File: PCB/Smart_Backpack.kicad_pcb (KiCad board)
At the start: 2 copper layers, 65.8 x 74.4 mm, 58 parts, among them J1 Conn_01x03_Pin, J2 Conn_01x02_Pin, J3 Conn_01x02_Pin, J4 Conn_01x03_Pin, J5 Conn_01x03_Pin, J6 Conn_01x03_Pin, J7 Conn_01x07_Pin, J8 Conn_01x08_Socket, J9 USB_C_Receptacle_USB2.0_16P, SW1 SW_Push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

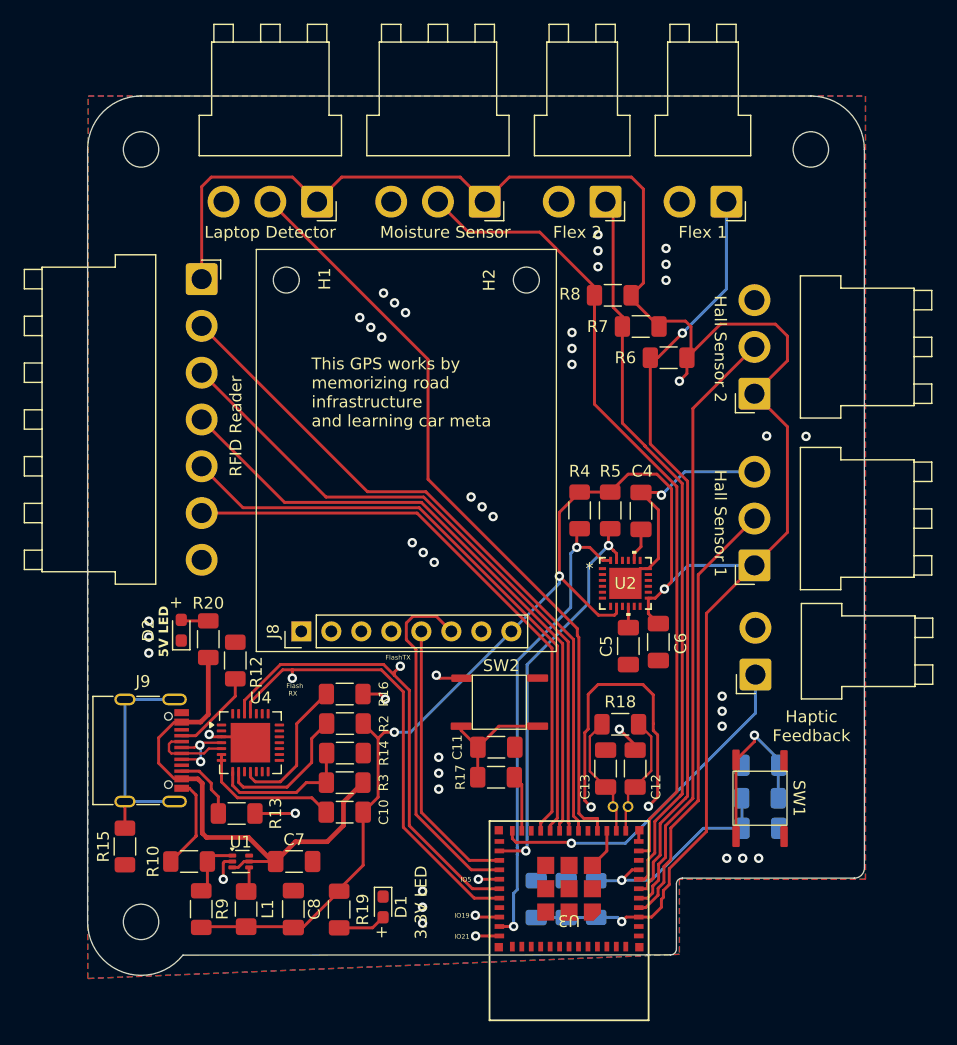
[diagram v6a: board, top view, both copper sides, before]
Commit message: fix silkscreen for motor connector
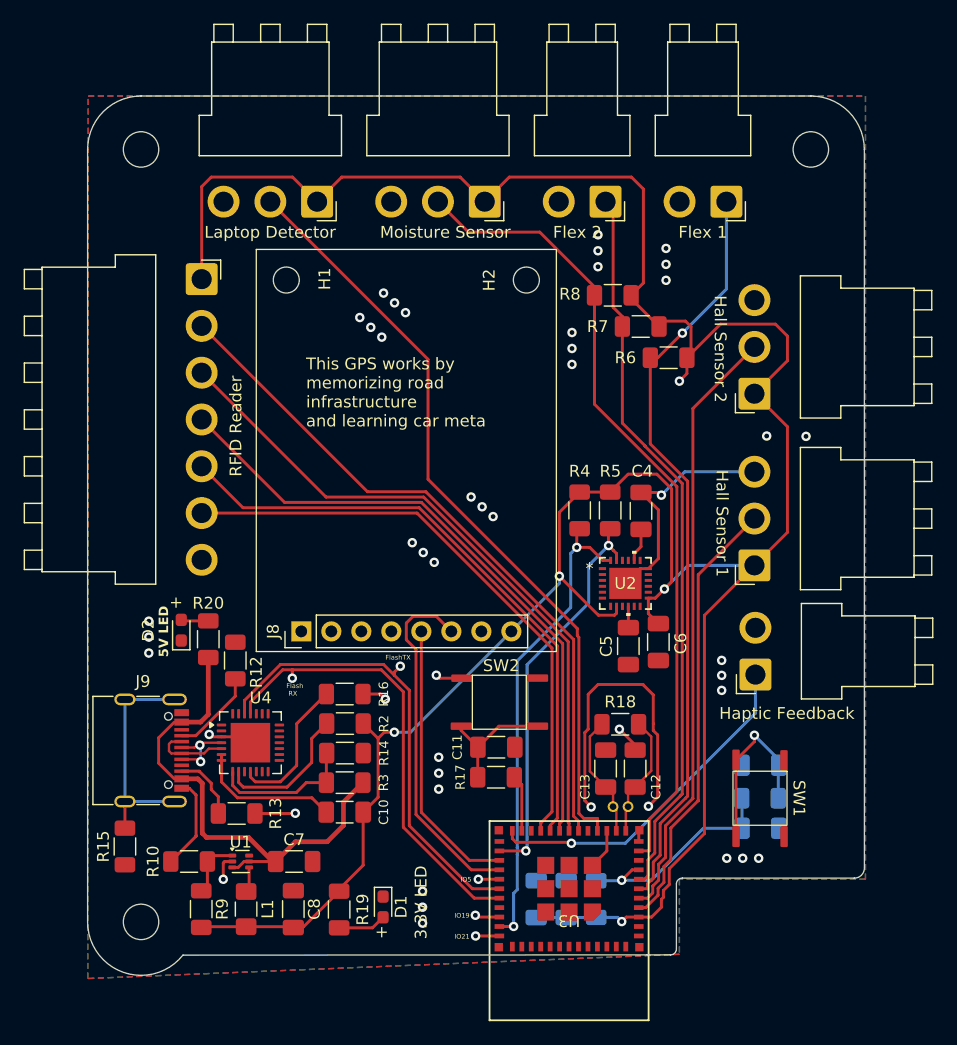
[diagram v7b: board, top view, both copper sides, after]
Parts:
- J10: renamed from Haptic Feedback
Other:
- board text removed: "Haptic Feedback"
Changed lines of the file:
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@@
 		)
 		(property "Label" "Hall Sensor 1"
-			(at 3.5536 -2.8956 270)
+			(at 3.5536 -2.742 270)
 			(unlocked yes)
 			(layer "F.SilkS")
@@
 		(descr "JST VH series connector, B2PS-VH (http://www.jst-mfg.com/product/pdf/eng/eVH.pdf), generated with kicad-footprint-generator")
 		(tags "connector JST VH horizontal")
-		(property "Reference" "Haptic Feedback"
+		(property "Reference" "J10"
 			(at -3.862 3.473 0)
 			(layer "F.SilkS")
@@
 			(at 1.98 16.1 90)
 			(layer "F.Fab")
+			(hide yes)
 			(effects
 				(font
@@
 			)
 		)
+		(property "Label" "Haptic Feedback"
+			(at -3.286 2.665 0)
+			(unlocked yes)
+			(layer "F.SilkS")
+			(effects
+				(font
+					(size 1 1)
+					(thickness 0.15)
+				)
+			)
+		)
 		(property ki_fp_filters "Connector*:*_1x??_*")
 		(sheetname "/Peripherals/")
@@
 	)
 	(gr_text "This GPS works by\nmemorizing road \ninfrastructure\nand learning car meta"
-		(at 104.24 67.71 0)
+		(at 103.78 67.71 0)
 		(layer "F.SilkS")
 		(effects
@@
 		)
 	)
-	(gr_text "Haptic \nFeedback\n"
-		(at 146.558 92.964 0)
-		(layer "F.SilkS")
-		(effects
-			(font
-				(size 1 1)
-				(thickness 0.15)
-			)
-		)
-	)
 	(gr_text "Smart Backpack\nMain Board\nRev. 1"
 		(at 124.17 68.92 0)
@@
 	)
 	(via
-		(at 139 91.694)
+		(at 138.96 88.66)
 		(size 0.8)
 		(drill 0.4)
@@
 	)
 	(via
-		(at 139 92.964)
+		(at 138.96 89.93)
 		(size 0.8)
 		(drill 0.4)
@@
 	)
 	(via
-		(at 139 90.424)
+		(at 138.96 87.39)
 		(size 0.8)
 		(drill 0.4)
@@
 	)
 	(segment
-		(start 134.027396 106.866034)
-		(end 134.524 106.36943)
-		(width 0.25)
-		(layer "F.Cu")
-		(net 10)
-	)
-	(segment
 		(start 116.82184 46.482)
 		(end 118.90464 48.5648)
@@
 	)
 	(segment
+		(start 133.858 107.61762)
+		(end 134.027396 107.448224)
+		(width 0.25)
+		(layer "F.Cu")
+		(net 10)
+	)
+	(segment
 		(start 143.51 58.928)
 		(end 138.8624 58.928)
@@
 	)
 	(segment
+		(start 134.524 106.36943)
+		(end 134.524 105.02505)
+		(width 0.25)
+		(layer "F.Cu")
+		(net 10)
+	)
+	(segment
 		(start 134.719 80.741689)
 		(end 134.719 72.87281)
@@
 	)
 	(segment
+		(start 134.524 105.02505)
+		(end 137.5 102.04905)
+		(width 0.25)
+		(layer "F.Cu")
+		(net 10)
+	)
+	(segment
 		(start 133.336774 82.123915)
 		(end 134.112 81.348689)
@@
 	)
 	(segment
-		(start 134.524 105.02505)
-		(end 137.668 101.88105)
+		(start 133.858 108.285199)
+		(end 133.858 107.61762)
 		(width 0.25)
 		(layer "F.Cu")
@@
 	)
 	(segment
-		(start 133.025198 109.118001)
-		(end 133.858 108.285199)
-		(width 0.25)
-		(layer "F.Cu")
-		(net 10)
-	)
-	(segment
 		(start 144.526 62.0244)
 		(end 144.526 59.944)
@@
 	)
 	(segment
+		(start 137.5 83.5792)
+		(end 141.732 79.3472)
+		(width 0.25)
+		(layer "F.Cu")
+		(net 10)
+	)
+	(segment
 		(start 102.7035 110.005)
 		(end 103.5045 110.005)
@@
 	)
 	(segment
-		(start 131.941996 109.118001)
-		(end 133.025198 109.118001)
-		(width 0.25)
-		(layer "F.Cu")
-		(net 10)
-	)
-	(segment
-		(start 134.027396 107.448224)
-		(end 134.027396 106.866034)
-		(width 0.25)
-		(layer "F.Cu")
-		(net 10)
-	)
-	(segment
-		(start 133.858 108.285199)
-		(end 133.858 107.61762)
-		(width 0.25)
-		(layer "F.Cu")
-		(net 10)
-	)
-	(segment
 		(start 144.526 76.5532)
 		(end 144.526 67.6124)
@@
 	)
 	(segment
-		(start 137.668 101.88105)
-		(end 137.668 83.4112)
-		(width 0.25)
-		(layer "F.Cu")
-		(net 10)
-	)
-	(segment
-		(start 133.858 107.61762)
-		(end 134.027396 107.448224)
+		(start 134.027396 107.448224)
+		(end 134.027396 106.866034)
 		(width 0.25)
 		(layer "F.Cu")
@@
 	)
 	(segment
-		(start 141.732 64.8184)
-		(end 144.526 62.0244)
+		(start 133.025198 109.118001)
+		(end 133.858 108.285199)
 		(width 0.25)
 		(layer "F.Cu")
@@
 	)
 	(segment
-		(start 136.362 61.4284)
-		(end 136.362 59.14064)
+		(start 141.732 64.8184)
+		(end 144.526 62.0244)
 		(width 0.25)
 		(layer "F.Cu")
@@
 	)
 	(segment
-		(start 137.668 83.4112)
-		(end 141.732 79.3472)
+		(start 136.362 61.4284)
+		(end 136.362 59.14064)
 		(width 0.25)
 		(layer "F.Cu")
@@
 	)
 	(segment
-		(start 134.524 106.36943)
-		(end 134.524 105.02505)
+		(start 134.112 81.348689)
+		(end 134.719 80.741689)
 		(width 0.25)
 		(layer "F.Cu")
@@
 	)
 	(segment
-		(start 134.112 81.348689)
-		(end 134.719 80.741689)
+		(start 110.4058 93.472)
+		(end 111.252 93.472)
 		(width 0.25)
 		(layer "F.Cu")
@@
 	)
 	(segment
-		(start 110.4058 93.472)
-		(end 111.252 93.472)
+		(start 134.027396 106.866034)
+		(end 134.524 106.36943)
 		(width 0.25)
 		(layer "F.Cu")
@@
 	)
 	(segment
+		(start 131.941996 109.118001)
+		(end 133.025198 109.118001)
+		(width 0.25)
+		(layer "F.Cu")
+		(net 10)
+	)
+	(segment
 		(start 108.622 92.739)
 		(end 109.8804 93.9974)
@@
 		(width 0.25)
 		(layer "F.Cu")
+		(net 10)
+	)
+	(segment
+		(start 137.5 102.04905)
+		(end 137.5 83.5792)
+		(width 0.25)
+		(layer "F.Cu")

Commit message: Alert: Fat inductor incoming
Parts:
- L1: footprint Inductor_SMD:L_1206_3216Metric_Pad1.42x1.75mm_HandSolder -> WeBench_Inductor:IND_BOURNS_SRN8040; moved to B.Cu
- moved L1 1.42 mm to (99.4, 107.2), turned to 0 degrees
